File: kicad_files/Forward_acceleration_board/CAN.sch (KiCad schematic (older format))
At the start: 2 parts

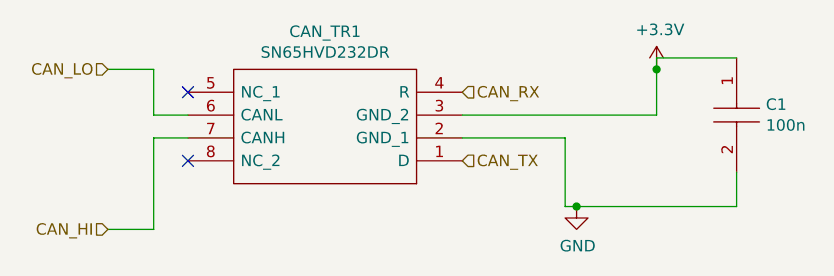
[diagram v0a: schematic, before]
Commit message: reogranized file locations, improved DSC controller pcb with edged margin on edges and rounded corners.  Completed Acceleration control board schematic
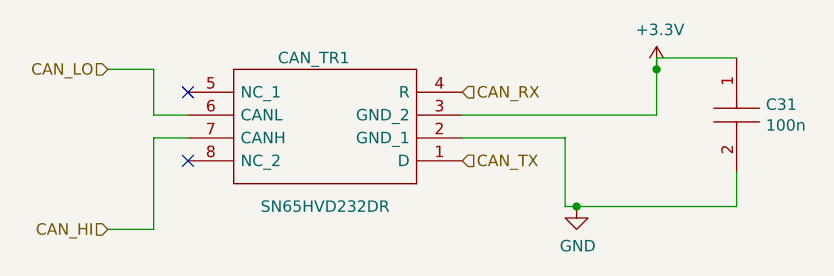
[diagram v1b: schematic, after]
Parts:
- renumbered C1 to C31
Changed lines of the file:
@@
 $Descr A4 11693 8268
 encoding utf-8
-Sheet 3 4
+Sheet 3 6
 Title ""
 Date ""
@@
 U 1 1 5D347533
 P 6450 3500
-F 0 "CAN_TR1" H 7050 2935 50  0000 C CNN
-F 1 "SN65HVD232DR" H 7050 3026 50  0000 C CNN
+F 0 "CAN_TR1" H 7100 3050 50  0000 C CNN
+F 1 "SN65HVD232DR" H 7050 3700 50  0000 C CNN
 F 2 "SN65HVD232DR:SOIC127P600X175-8N" H 7500 3600 50  0001 L CNN
 F 3 "http://www.ti.com/lit/gpn/sn65hvd232" H 7500 3500 50  0001 L CNN
@@
 	5100 3800 4900 3800
 $Comp
-L AS0805KKX7R0BB104:AS0805KKX7R0BB104 C1
+L AS0805KKX7R0BB104:AS0805KKX7R0BB104 C31
 U 1 1 5D347B38
 P 7650 3050
-F 0 "C1" V 7854 3178 50  0000 L CNN
+F 0 "C31" V 7854 3178 50  0000 L CNN
 F 1 "100n" V 7945 3178 50  0000 L CNN
 F 2 "AS0805KKX7R0BB104:CAPC2012X145N" H 8000 3100 50  0001 L CNN
